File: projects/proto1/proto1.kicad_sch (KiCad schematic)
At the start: 8 parts

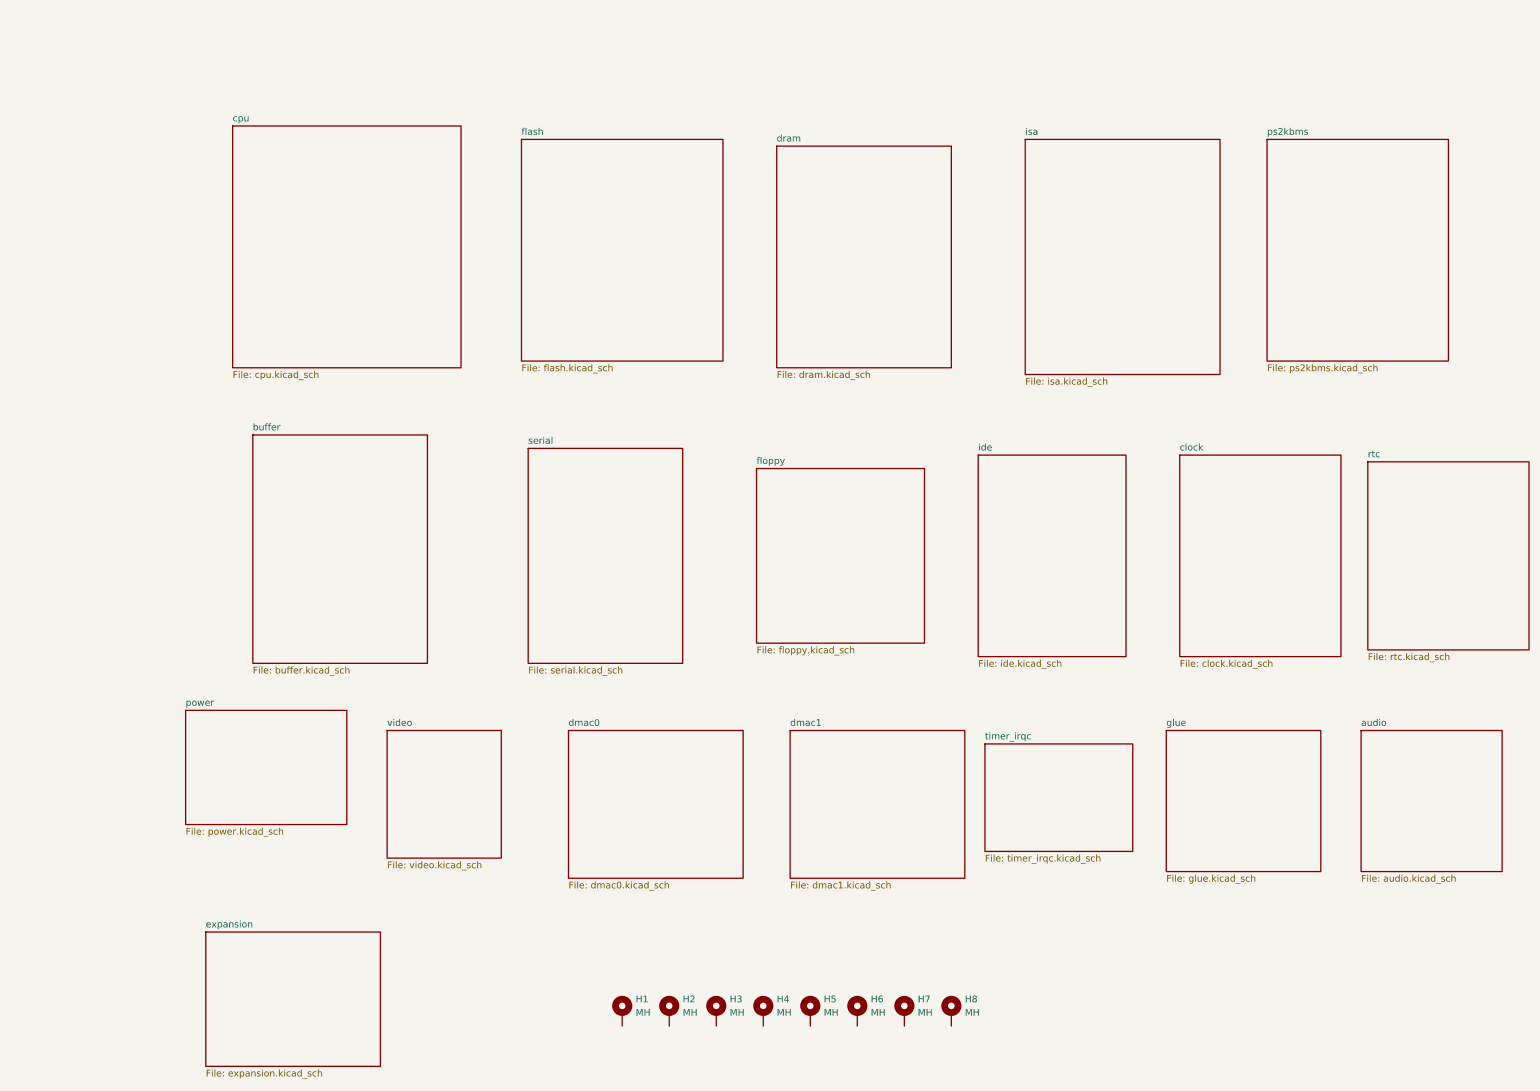
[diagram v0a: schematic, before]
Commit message: Renamed CMC to SCU, changed verification method to cocotb, and modified pcb schematic
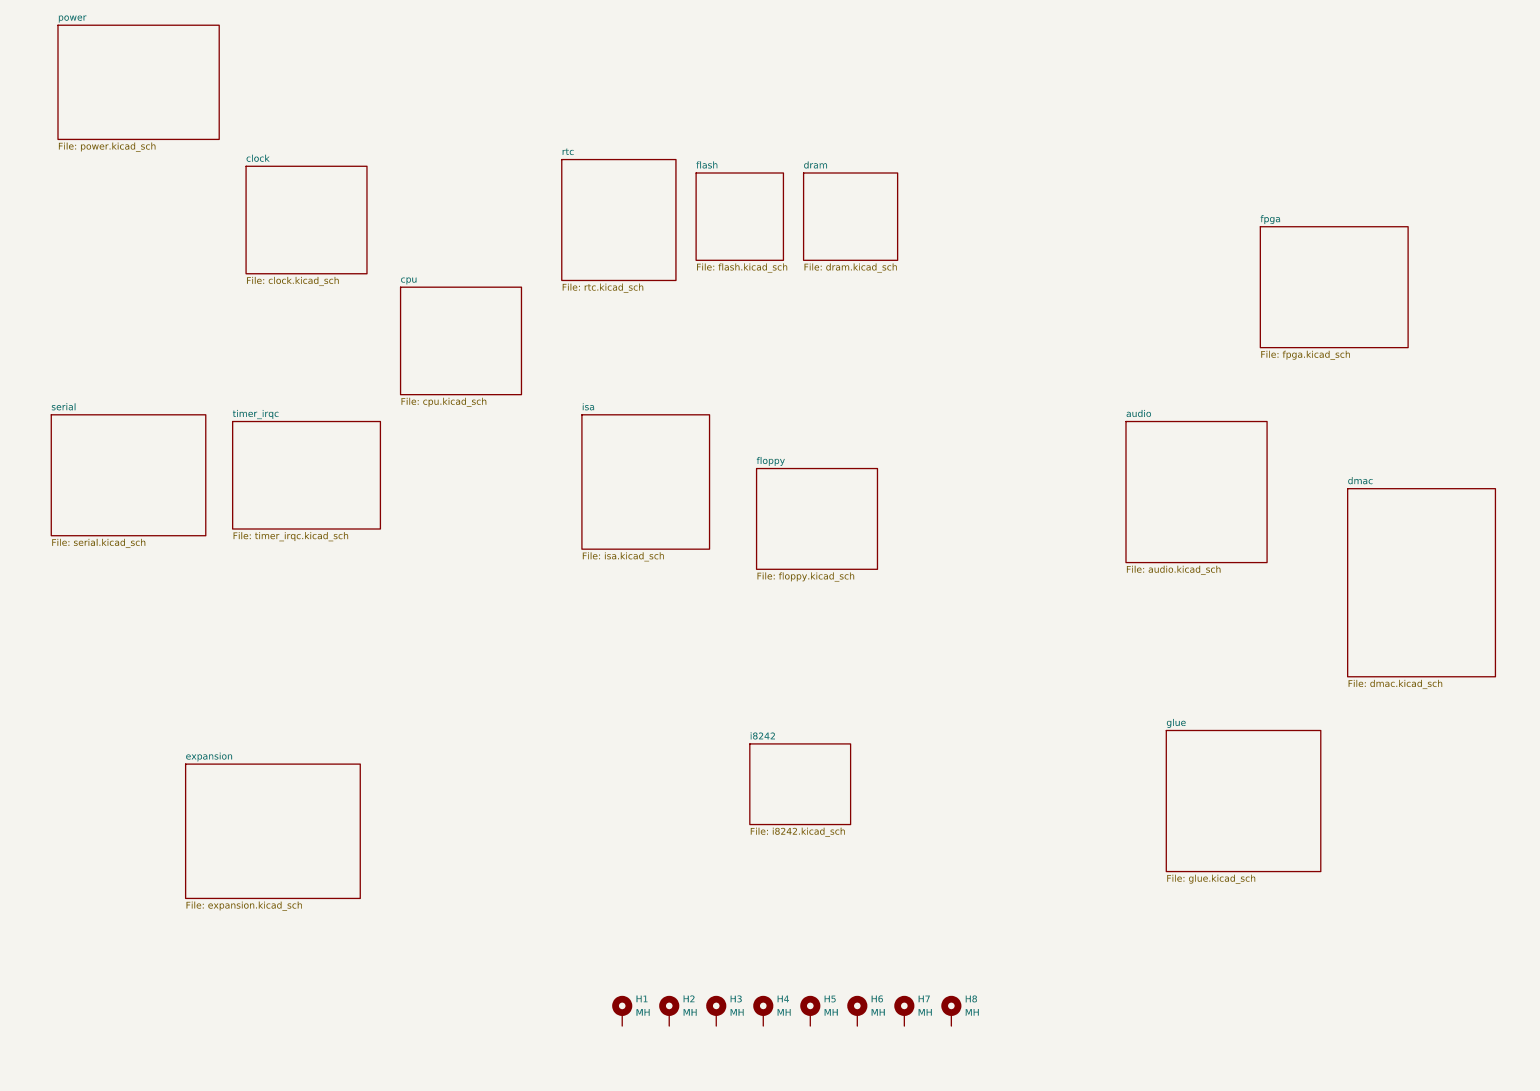
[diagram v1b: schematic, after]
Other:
- sheet ps2kbms renamed i8242
- removed sheet buffer
- removed sheet dmac0
- removed sheet dmac1
- removed sheet ide
- removed sheet video
- added sheet dmac (dmac.kicad_sch)
- added sheet fpga (fpga.kicad_sch)
- sheet i8242: file ps2kbms.kicad_sch -> i8242.kicad_sch

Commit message: Added timer and interrupt controller capability to SCU
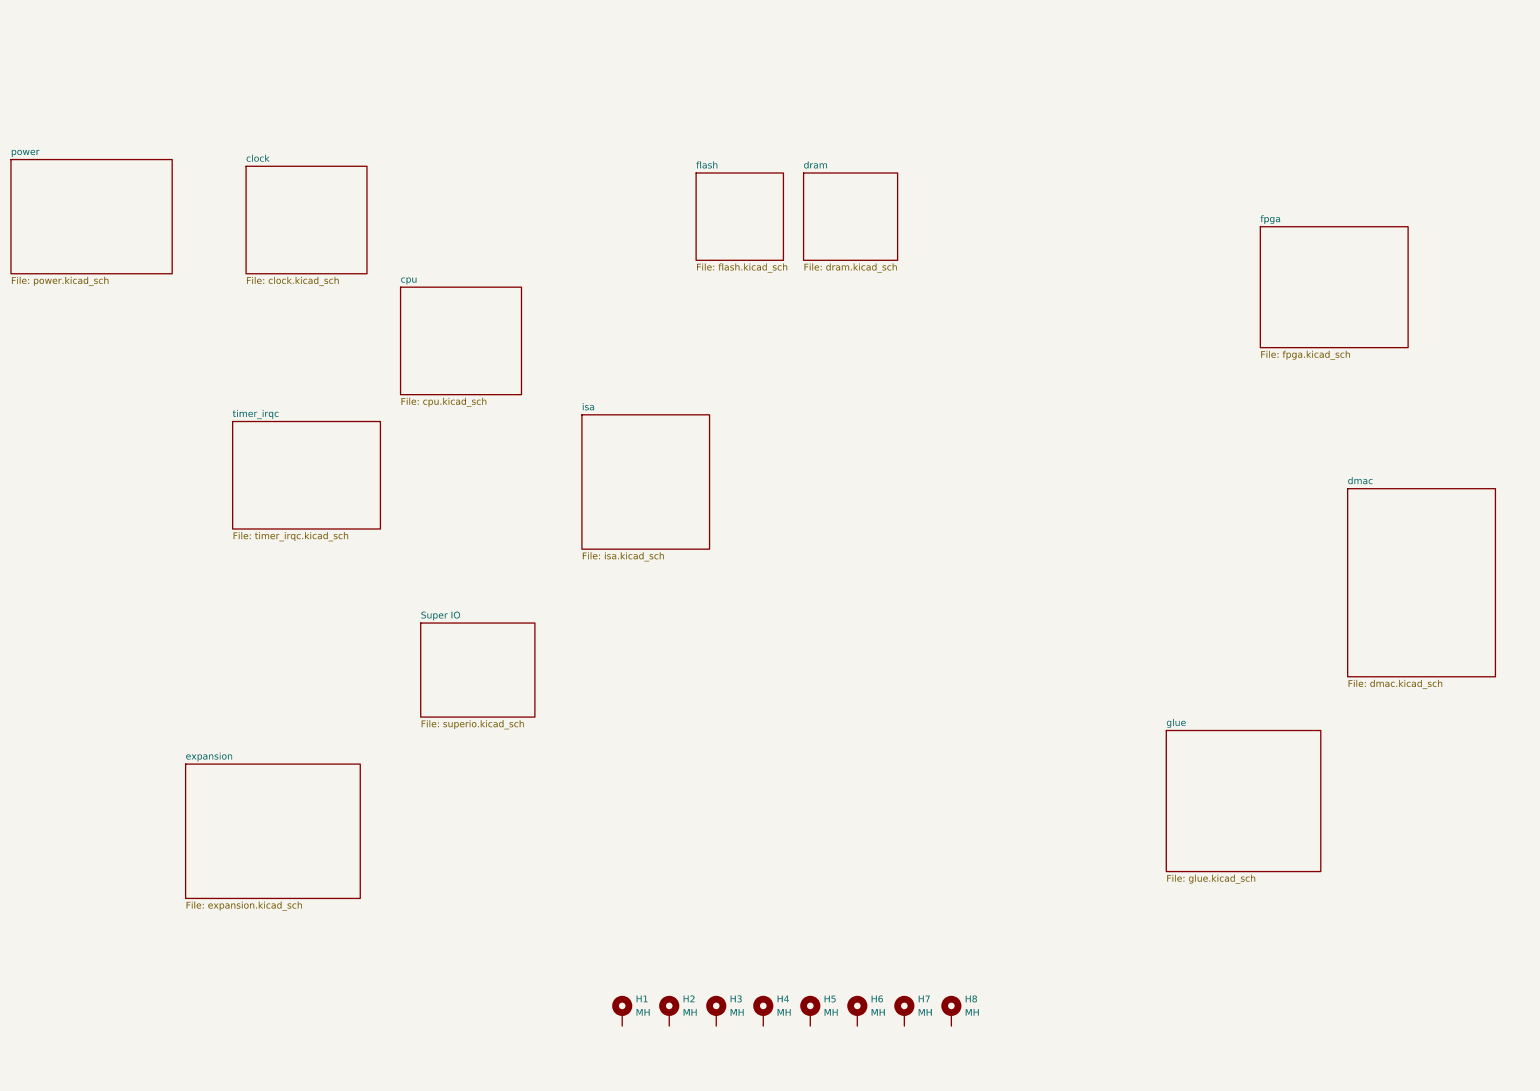
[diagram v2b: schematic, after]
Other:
- removed sheet audio
- removed sheet floppy
- removed sheet i8242
- removed sheet rtc
- removed sheet serial
- added sheet Super IO (superio.kicad_sch)
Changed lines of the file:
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@@
-	)
-	(sheet
-		(at 91.44 25.4)
-		(size 21.59 22.86)
-		(fields_autoplaced yes)
-		(stroke
-			(width 0.1524)
-			(type solid)
-		)
-		(fill
-			(color 0 0 0 0.0000)
-		)
-		(property "Sheetname" "rtc"
-			(at 91.44 24.6884 0)
-			(effects
-				(font
-					(size 1.27 1.27)
-				)
-				(justify left bottom)
-			)
-		)
-		(property "Sheetfile" "rtc.kicad_sch"
-			(at 91.44 48.8446 0)
-			(effects
-				(font
-					(size 1.27 1.27)
-				)
-				(justify left top)
-			)
-		)
-		(instances
-			(project "proto1"
-				(path "/e910d5a4-fa64-450e-b748-cf3a61fb2249"
-					(page "13")
-				)
-			)
-		)
 	)
 	(sheet
@@
 	)
 	(sheet
-		(at -3.81 0)
+		(at -12.7 25.4)
 		(size 30.48 21.59)
 		(fields_autoplaced yes)
@@
 		)
 		(property "Sheetname" "power"
-			(at -3.81 -0.7116 0)
+			(at -12.7 24.6884 0)
 			(effects
 				(font
@@
 		)
 		(property "Sheetfile" "power.kicad_sch"
-			(at -3.81 22.1746 0)
+			(at -12.7 47.5746 0)
 			(effects
 				(font
@@
 				(path "/e910d5a4-fa64-450e-b748-cf3a61fb2249"
 					(page "12")
-				)
-			)
-		)
-	)
-	(sheet
-		(at 128.27 83.82)
-		(size 22.86 19.05)
-		(fields_autoplaced yes)
-		(stroke
-			(width 0.1524)
-			(type solid)
-		)
-		(fill
-			(color 0 0 0 0.0000)
-		)
-		(property "Sheetname" "floppy"
-			(at 128.27 83.1084 0)
-			(effects
-				(font
-					(size 1.27 1.27)
-				)
-				(justify left bottom)
-			)
-		)
-		(property "Sheetfile" "floppy.kicad_sch"
-			(at 128.27 103.4546 0)
-			(effects
-				(font
-					(size 1.27 1.27)
-				)
-				(justify left top)
-			)
-		)
-		(instances
-			(project "proto1"
-				(path "/e910d5a4-fa64-450e-b748-cf3a61fb2249"
-					(page "8")
 				)
 			)
@@
 	)
 	(sheet
-		(at 127 135.89)
-		(size 19.05 15.24)
-		(fields_autoplaced yes)
-		(stroke
-			(width 0.1524)
-			(type solid)
-		)
-		(fill
-			(color 0 0 0 0.0000)
-		)
-		(property "Sheetname" "i8242"
-			(at 127 135.1784 0)
-			(effects
-				(font
-					(size 1.27 1.27)
-				)
-				(justify left bottom)
-			)
-		)
-		(property "Sheetfile" "i8242.kicad_sch"
-			(at 127 151.7146 0)
-			(effects
-				(font
-					(size 1.27 1.27)
-				)
-				(justify left top)
-			)
-		)
-		(instances
-			(project "proto1"
-				(path "/e910d5a4-fa64-450e-b748-cf3a61fb2249"
-					(page "10")
-				)
-			)
-		)
-	)
-	(sheet
 		(at 116.84 27.94)
 		(size 16.51 16.51)
@@
 	)
 	(sheet
-		(at 198.12 74.93)
-		(size 26.67 26.67)
-		(fields_autoplaced yes)
-		(stroke
-			(width 0.1524)
-			(type solid)
-		)
-		(fill
-			(color 0 0 0 0.0000)
-		)
-		(property "Sheetname" "audio"
-			(at 198.12 74.2184 0)
-			(effects
-				(font
-					(size 1.27 1.27)
-				)
-				(justify left bottom)
-			)
-		)
-		(property "Sheetfile" "audio.kicad_sch"
-			(at 198.12 102.1846 0)
-			(effects
-				(font
-					(size 1.27 1.27)
-				)
-				(justify left top)
-			)
-		)
-		(instances
-			(project "proto1"
-				(path "/e910d5a4-fa64-450e-b748-cf3a61fb2249"
-					(page "19")
-				)
-			)
-		)
-	)
-	(sheet
-		(at -5.08 73.66)
-		(size 29.21 22.86)
-		(fields_autoplaced yes)
-		(stroke
-			(width 0.1524)
-			(type solid)
-		)
-		(fill
-			(color 0 0 0 0.0000)
-		)
-		(property "Sheetname" "serial"
-			(at -5.08 72.9484 0)
-			(effects
-				(font
-					(size 1.27 1.27)
-				)
-				(justify left bottom)
-			)
-		)
-		(property "Sheetfile" "serial.kicad_sch"
-			(at -5.08 97.1046 0)
-			(effects
-				(font
-					(size 1.27 1.27)
-				)
-				(justify left top)
-			)
-		)
-		(instances
-			(project "proto1"
-				(path "/e910d5a4-fa64-450e-b748-cf3a61fb2249"
-					(page "7")
-				)
-			)
-		)
-	)
-	(sheet
 		(at 95.25 73.66)
 		(size 24.13 25.4)
@@
 				)
 			)
+		)
+	)
+	(sheet
+		(at 64.77 113.03)
+		(size 21.59 17.78)
+		(fields_autoplaced yes)
+		(stroke
+			(width 0.1524)
+			(type solid)
+		)
+		(fill
+			(color 0 0 0 0.0000)
+		)
+		(property "Sheetname" "Super IO"
+			(at 64.77 112.3184 0)
+			(effects
+				(font
+					(size 1.27 1.27)
+				)
+				(justify left bottom)
+			)
+		)
+		(property "Sheetfile" "superio.kicad_sch"
+			(at 64.77 131.3946 0)
+			(effects
+				(font
+					(size 1.27 1.27)
+				)
+				(justify left top)
+			)
+		)
+		(instances
+			(project "proto1"
+				(path "/e910d5a4-fa64-450e-b748-cf3a61fb2249"
+					(page "27")
+				)
+			)
